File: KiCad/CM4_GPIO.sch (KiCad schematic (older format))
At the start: 16 parts, among them J16 GSD090012SEU, J17 Conn_02x04_Odd_Even, J18 RJMG2012119A0NR, J19 Conn_02x20_Odd_Even, J20 Conn_02x04_Odd_Even, U6 74LVC1G07GW,125, U7 TPD4EUSB30, U8 RT9742GGJ5, U9 TPD4EUSB30

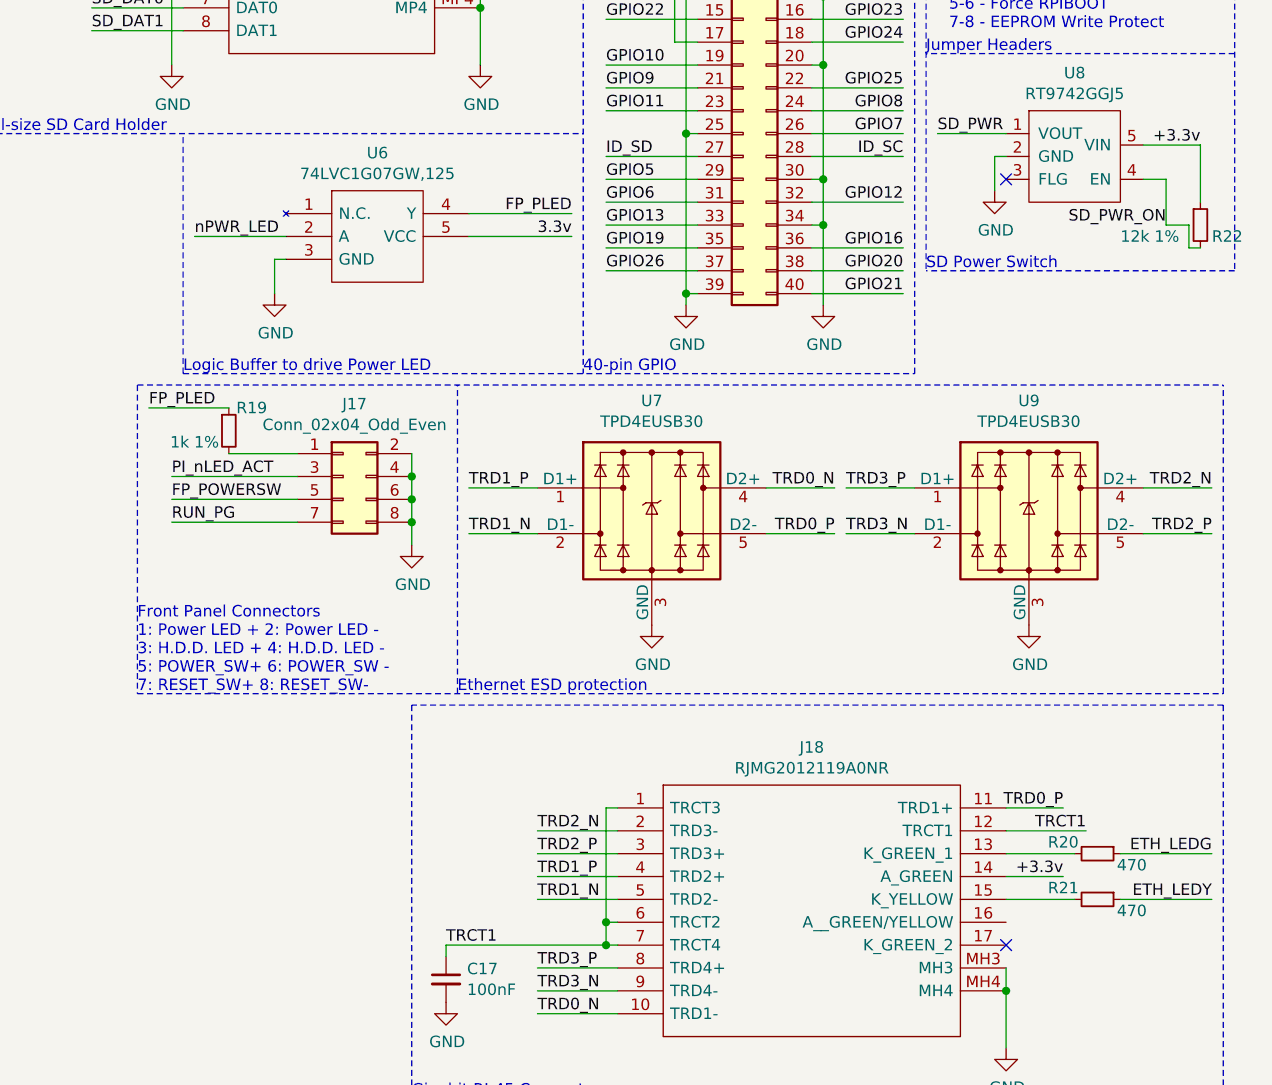
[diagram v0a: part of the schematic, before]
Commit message: Small changes to PCIe, USB Schematics and board layout, legend for GPIO pins.
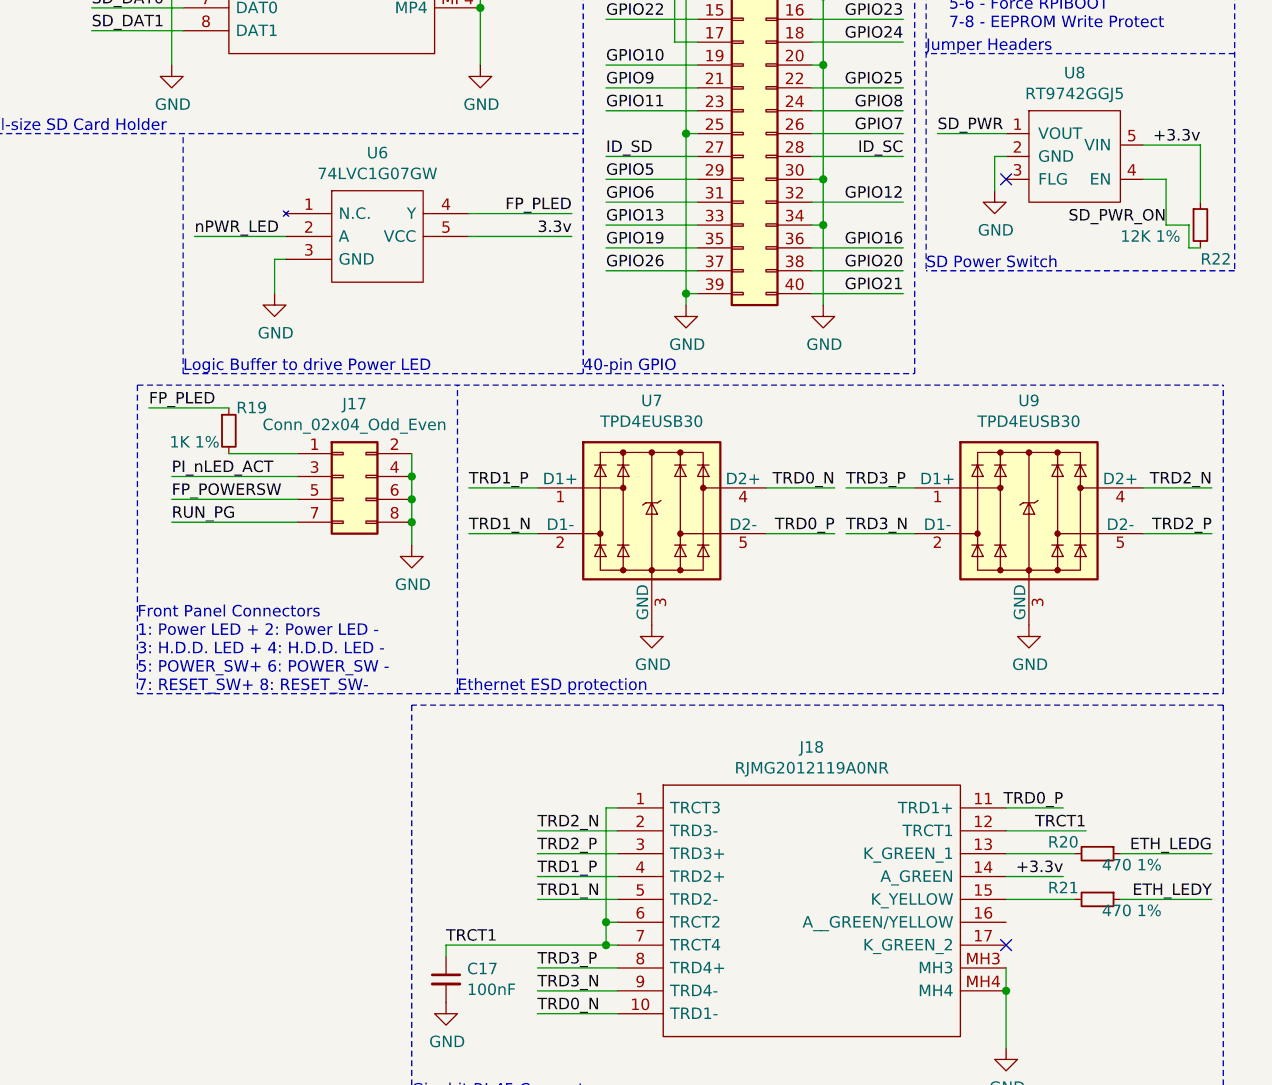
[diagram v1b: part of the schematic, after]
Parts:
- J17, J20: footprint CM4_MATX:PinHeader_2x04_P1.00mm_Vertical -> CM4_MATX:PinHeader_2x04_P2.54mm_Vertical
- J19: footprint CM4_MATX:PinHeader_2x20_P1.00mm_Vertical -> CM4_MATX:PinHeader_2x20_P2.54mm_Vertical
- R19: value 1k 1% -> 1K 1%
- R20, R21: value 470 -> 470 1%
- R22: value 12k 1% -> 12K 1%
- U6: value 74LVC1G07GW,125 -> 74LVC1G07GW
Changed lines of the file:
@@
 $Descr A4 11693 8268
 encoding utf-8
-Sheet 7 8
-Title ""
-Date ""
-Rev ""
-Comp ""
-Comment1 ""
+Sheet 6 10
+Title "GPIO, SDIO, PIn Headers, Ethernet"
+Date "2020-11-27"
+Rev "0.1"
+Comp "CM4_MATX Contributors"
+Comment1 "https://github.com/theguydanish/CM4_MATX"
 Comment2 ""
 Comment3 ""
@@
 F 0 "J20" H 10750 1167 50  0000 C CNN
 F 1 "Conn_02x04_Odd_Even" H 10750 1076 50  0000 C CNN
-F 2 "CM4_MATX:PinHeader_2x04_P1.00mm_Vertical" H 10700 850 50  0001 C CNN
+F 2 "CM4_MATX:PinHeader_2x04_P2.54mm_Vertical" H 10700 850 50  0001 C CNN
 F 3 "~" H 10700 850 50  0001 C CNN
 	1    10700 850
@@
 F 0 "J19" H 9100 2767 50  0000 C CNN
 F 1 "Conn_02x20_Odd_Even" H 9100 2676 50  0000 C CNN
-F 2 "CM4_MATX:PinHeader_2x20_P1.00mm_Vertical" H 9050 1650 50  0001 C CNN
+F 2 "CM4_MATX:PinHeader_2x20_P2.54mm_Vertical" H 9050 1650 50  0001 C CNN
 F 3 "~" H 9050 1650 50  0001 C CNN
 	1    9050 1650
@@
 P 10600 5100
 F 0 "R20" V 10550 4950 50  0000 C CNN
-F 1 "470" V 10650 5250 50  0000 C CNN
+F 1 "470 1%" V 10650 5250 50  0000 C CNN
 F 2 "" H 10600 5100 50  0001 C CNN
 F 3 "~" H 10600 5100 50  0001 C CNN
@@
 P 10600 5300
 F 0 "R21" V 10550 5150 50  0000 C CNN
-F 1 "470" V 10650 5450 50  0000 C CNN
+F 1 "470 1%" V 10650 5450 50  0000 C CNN
 F 2 "" H 10600 5300 50  0001 C CNN
 F 3 "~" H 10600 5300 50  0001 C CNN
@@
 U 1 1 6014DF99
 P 11050 2350
-F 0 "R22" H 11100 2300 50  0000 L CNN
-F 1 "12k 1%" H 10700 2300 50  0000 L CNN
+F 0 "R22" H 11050 2200 50  0000 L CNN
+F 1 "12K 1%" H 10700 2300 50  0000 L CNN
 F 2 "" H 11050 2350 50  0001 C CNN
 F 3 "~" H 11050 2350 50  0001 C CNN
@@
 P 7050 2300
 F 0 "U6" H 7450 2565 50  0000 C CNN
-F 1 "74LVC1G07GW,125" H 7450 2474 50  0000 C CNN
+F 1 "74LVC1G07GW" H 7450 2474 50  0000 C CNN
 F 2 "CM4_MATX:SOT65P212X110-5N" H 8000 2400 50  0001 L CNN
 F 3 "https://assets.nexperia.com/documents/data-sheet/74LVC1G07.pdf" H 8000 2300 50  0001 L CNN
@@
 F 0 "J17" H 7350 3767 50  0000 C CNN
 F 1 "Conn_02x04_Odd_Even" H 7350 3676 50  0000 C CNN
-F 2 "CM4_MATX:PinHeader_2x04_P1.00mm_Vertical" H 7300 3450 50  0001 C CNN
+F 2 "CM4_MATX:PinHeader_2x04_P2.54mm_Vertical" H 7300 3450 50  0001 C CNN
 F 3 "~" H 7300 3450 50  0001 C CNN
 	1    7300 3450
@@
 P 6800 3250
 F 0 "R19" H 6900 3350 50  0000 C CNN
-F 1 "1k 1%" H 6650 3200 50  0000 C CNN
+F 1 "1K 1%" H 6650 3200 50  0000 C CNN
 F 2 "" H 6800 3250 50  0001 C CNN
 F 3 "~" H 6800 3250 50  0001 C CNN

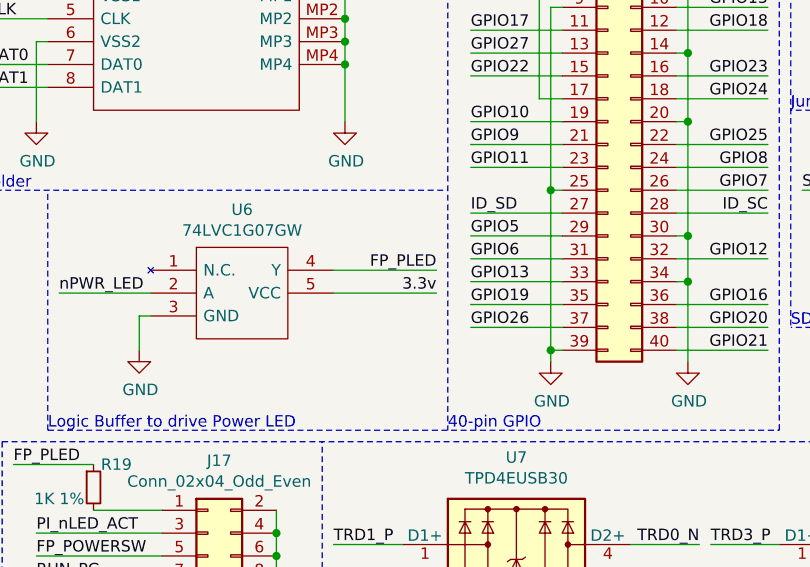
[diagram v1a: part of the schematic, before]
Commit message: Added License text, fixes #30, updated PCB to include copyright notice.
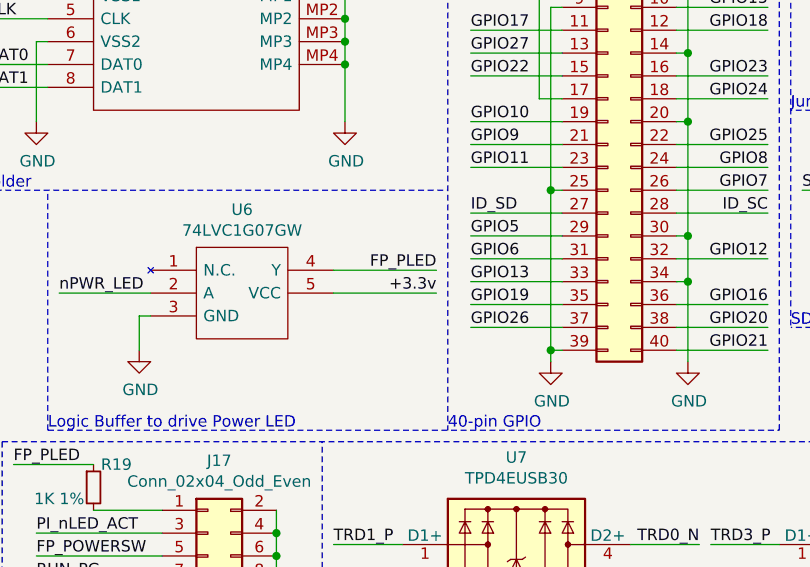
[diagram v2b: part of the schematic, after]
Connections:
- net 3.3v is gone; now on net +3.3v: U6.5 (VCC)
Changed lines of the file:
@@
 Sheet 6 10
 Title "GPIO, SDIO, PIn Headers, Ethernet"
-Date "2020-11-27"
+Date "2020-12-14"
 Rev "0.1"
-Comp "CM4_MATX Contributors"
+Comp "Copyright Oliver Møller/@TheGuyDanish 2020, CERN OHL-P v2"
 Comment1 "https://github.com/theguydanish/CM4_MATX"
 Comment2 ""
@@
 U 1 1 5FBC3653
 P 5650 1000
+AR Path="/5FBC3653" Ref="Module1"  Part="1"
+AR Path="/5FBC336F/5FBC3653" Ref="Module1"  Part="1"
 F 0 "Module1" H 2800 1100 50  0000 C CNN
 F 1 "ComputeModule4-CM4" H 2800 1000 50  0000 C CNN
@@
 $EndComp
 Text Label 8300 2400 2    50   ~ 0
-3.3v
++3.3v
 Text Label 8300 2300 2    50   ~ 0
 FP_PLED
